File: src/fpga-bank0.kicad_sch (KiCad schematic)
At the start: 21 parts

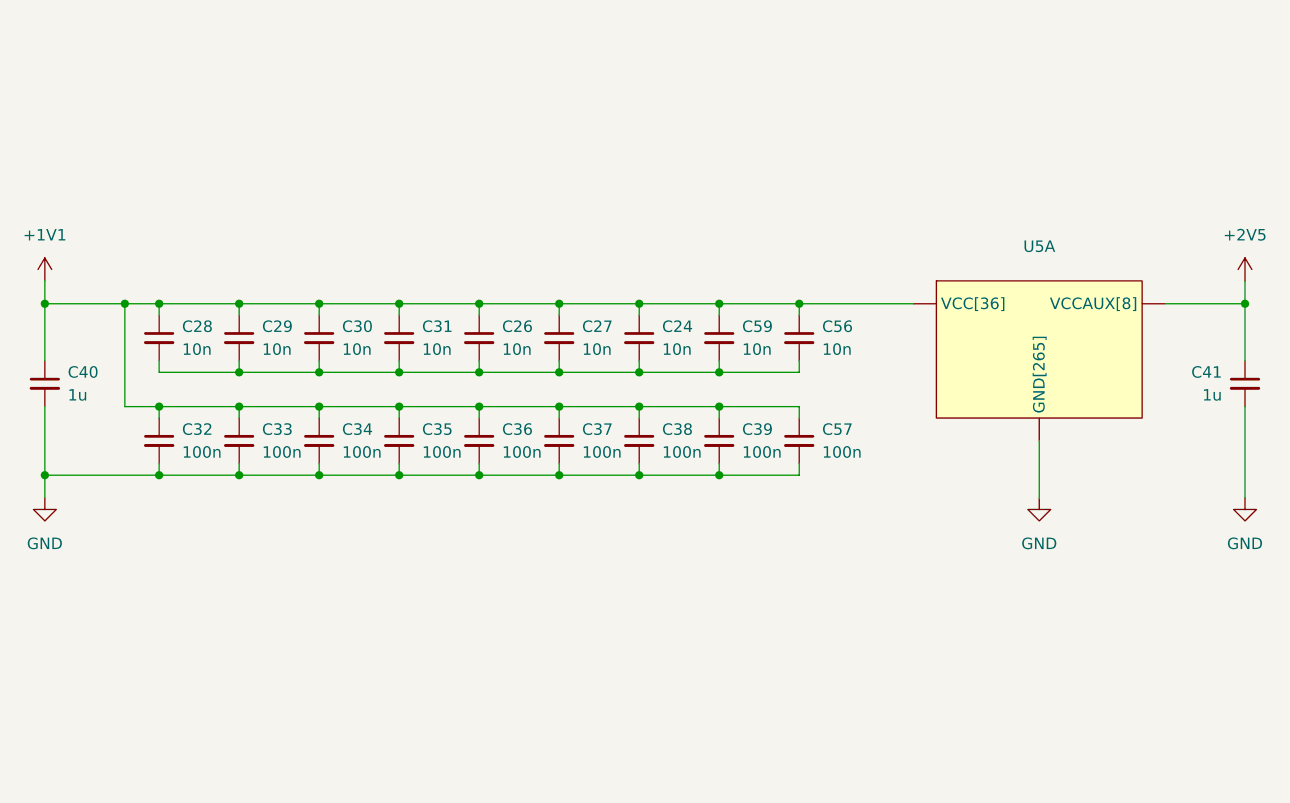
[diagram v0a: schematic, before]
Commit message: Adds more FPGA IO banks
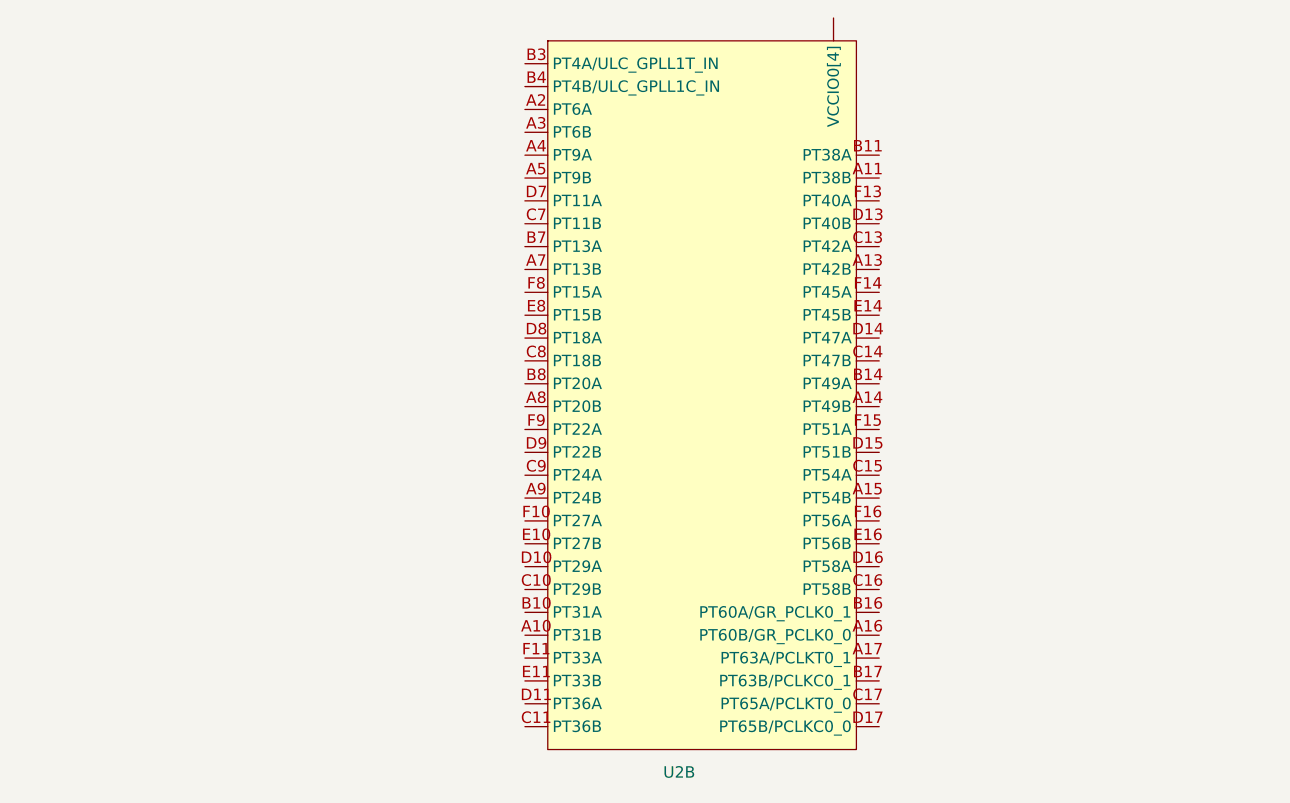
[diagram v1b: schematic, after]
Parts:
- removed C24, C26, C27, C28, C29, C30, C31, C56, C59: 10n, symbol Device:C_Small
- removed C32, C33, C34, C35, C36, C37, C38, C39, C57: 100n, symbol Device:C_Small
- removed C40, C41: 1u, symbol Device:C_Small
- removed U5: ~, symbol ECAP5-BSOM:LFE5U-85F-*BG756*
- added U2: ~, symbol ECAP5-BSOM:LFE5U-85F-*BG756*
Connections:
- new net VCCIO0: U2. (VCCIO0[4]), U2.K12 (VCCIO0), U2.K14 (VCCIO0), U2.K15 (VCCIO0), U2.K16 (VCCIO0)
